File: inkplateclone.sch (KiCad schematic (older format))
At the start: 43 parts, among them J1 ED060SC7, J2 Conn_01x16_Male, U1 TPS65186, U2 ED097OC1, U3 MCP23017_SO

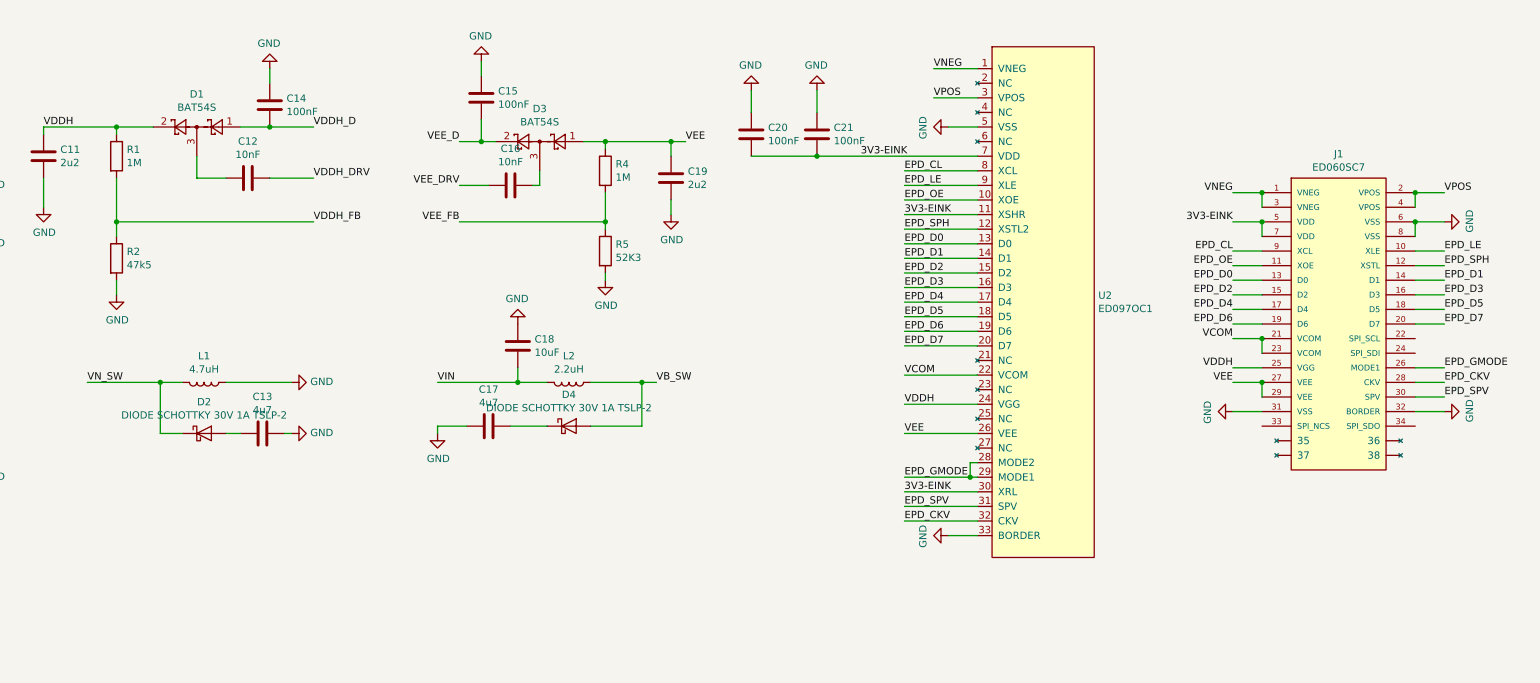
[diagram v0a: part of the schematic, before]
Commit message: added SPI pullup resistors for the 6inch display
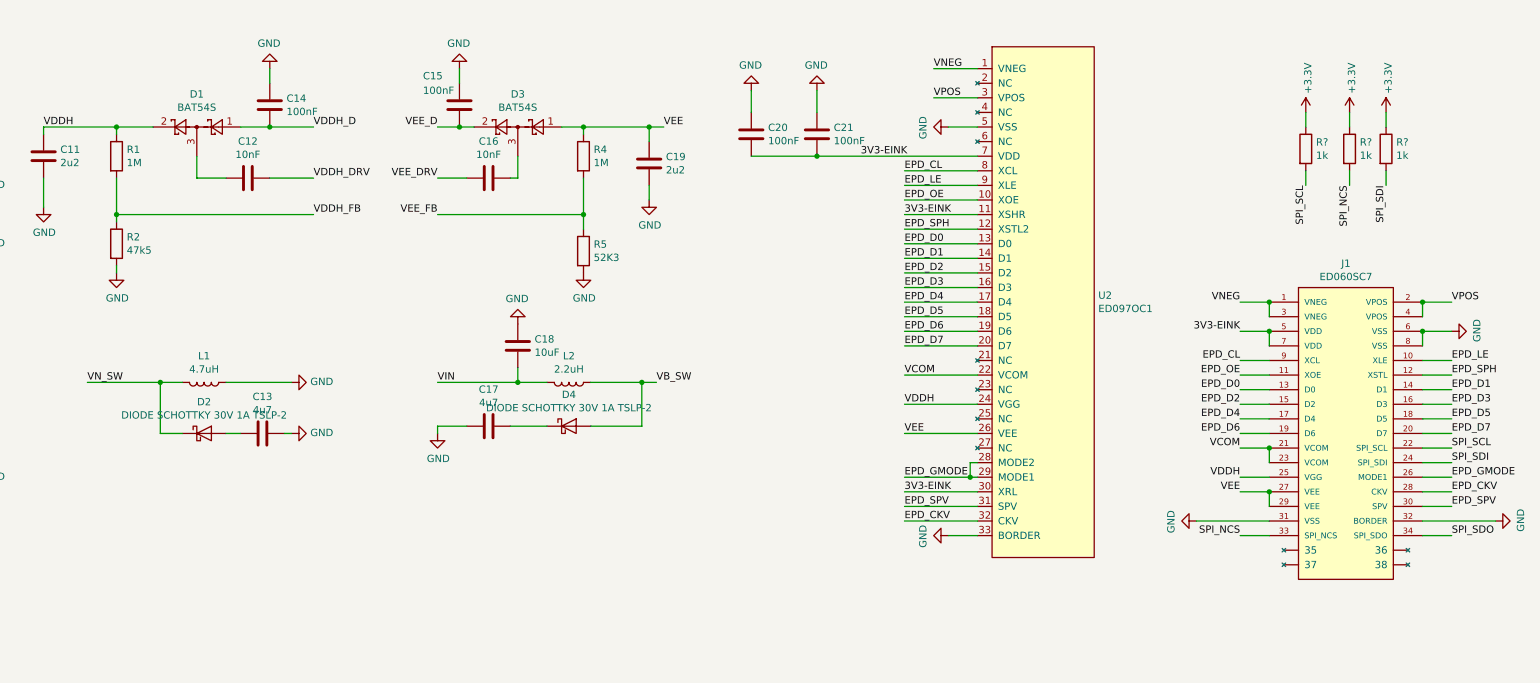
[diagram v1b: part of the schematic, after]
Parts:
- added R? (x3): 1k, Resistor_SMD:R_0805_2012Metric, symbol Device:R
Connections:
- net labels added: SPI_NCS, SPI_SCL, SPI_SDI, SPI_SDO
- wire segments 212 -> 220
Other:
- moved on the sheet: C15, C16, C19, D3, J1, R2, R4, R5

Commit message: wiring up the Wrover, WIP
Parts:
- added C23: 10uF, Capacitor_SMD:C_1206_3216Metric, symbol Device:C
- added C24: 2u2, Capacitor_SMD:C_0805_2012Metric, symbol Device:C
- added C25, C27: 68uF, 6.3v, Capacitor_Tantalum_SMD:CP_EIA-3528-15_AVX-H_Pad1.50x2.35mm_HandSolder, symbol Device:CP
- added C26, C28: 100nF, Capacitor_SMD:C_0805_2012Metric, symbol Device:C
- added U4: ESP32-WROVER, Wrover:ESP32-WROVER, symbol Wrover:ESP32-WROVER
- J1: footprint PANASONIC_AXT334124 -> inkplateclone:PANASONIC_AXT334124
- gave numbers to parts that had none: 3
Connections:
- net labels added: RST, RXD, TXD
- wire segments 220 -> 254

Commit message: ripped up and made a mess but its cool. Also added cooling pad underneath TPS56186 chip
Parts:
- removed J2: Conn_01x16_Male, Connector_PinSocket_2.54mm:PinSocket_1x16_P2.54mm_Horizontal, symbol Connector:Conn_01x16_Male
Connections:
- wire segments 254 -> 238
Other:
- moved on the sheet: C23, C24, C25, C26, C27, C28, U4

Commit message: added usb C-serial and fixed errors in the tps65186 part of the schematic
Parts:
- added C29: 100nF, Capacitor_SMD:C_0805_2012Metric, symbol Device:C
- added J2: USB_C_Receptacle_USB2.0, Connector_USB:USB_C_Receptacle_HRO_TYPE-C-31-M-12, symbol Connector:USB_C_Receptacle_USB2.0
- added Q1, Q2: Q_NMOS_GSD, Package_TO_SOT_SMD:SOT-23, symbol Device:Q_NMOS_GSD
- added R13, R14: 5.1K, Resistor_SMD:R_0805_2012Metric, symbol Device:R
- added R15, R16, R17, R18: 10K, Resistor_SMD:R_0805_2012Metric, symbol Device:R
- added U5: CH340C, Package_SO:SOIC-16_3.9x9.9mm_P1.27mm, symbol Interface_USB:CH340G
- U1: footprint Package_DFN_QFN:QFN-48-1EP_7x7mm_P0.5mm_EP5.3x5.3mm -> TP56186:QFN-48-1EP_7x7mm_P0.5mm_EP5.3x5.3mm_ThermalVias
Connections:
- net +3V3: now also R17.2, R18.2
- net EPD_CL: now also Q2.3 (D), R18.1
- net GND: now also J1.~ (38), C29.1, J2.A1 (GND), J2.A12 (GND), J2.B1 (GND), J2.B12 (GND), J2.S1 (SHIELD), R13.1, R14.1, U5.1 (GND)
- net RST: now also Q1.3 (D), R17.1
- net VB: now also C17.1, D4.1 (K)
- net VIN: now also C4.1, U1.10 (VIN)
- net VN: now also C13.2, D2.2 (A)
- net RXD renamed ESP_RXD
- net ESP_RXD: now also U5.2 (TXD)
- net TXD renamed ESP_TXD
- net ESP_TXD: now also U5.3 (RXD)
- new net: J2.A5 (CC1), R13.2
- new net: J2.B5 (CC2), R14.2
- new net: Q2.1 (G), R16.1
- new net: Q1.1 (G), R15.1
- new net +5V: C29.2, J2.A4 (VBUS), J2.A9 (VBUS), J2.B4 (VBUS), J2.B9 (VBUS), U5.16 (VCC)
- new net SER_DTR: Q2.2 (S), R15.2, U5.13 (~DTR)
- new net SER_RTS: Q1.2 (S), R16.2, U5.14 (~RTS)
- new net USB_DN: J2.A7 (D-), J2.B7 (D-), U5.6 (UD-)
- new net USB_DP: J2.A6 (D+), J2.B6 (D+), U5.5 (UD+)
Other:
- moved on the sheet: C22, R8, R9, U3

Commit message: added ideal diode and 3.3v circuit. Battery stuff and inputs still todo
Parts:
- added C30, C32, C33, C35: 4u7, Capacitor_SMD:C_0805_2012Metric, symbol Device:C
- added C31, C34: 100nF, Capacitor_SMD:C_0805_2012Metric, symbol Device:C
- added D5: BAT20JFILM, Diode_SMD:D_SOD-323, symbol Device:D_Schottky
- added Q3: Q_PMOS_GSD, Package_TO_SOT_SMD:SOT-23, symbol Device:Q_PMOS_GSD
- added R19: 10K, Resistor_SMD:R_0805_2012Metric, symbol Device:R
- added U6: AMS1117-3.3, Package_TO_SOT_SMD:SOT-223-3_TabPin2, symbol Regulator_Linear:AMS1117-3.3
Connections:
- net +3V3: now also C33.2, C34.2, C35.2, U6.2 (VO)
- net +5V: now also D5.2 (A), Q3.1 (G), R19.2
- net GND: now also C30.1, C31.1, C32.1, C33.1, C34.1, C35.1, R19.1, U6.1 (GND)
- net VIN renamed VCC
- net VCC: now also C30.2, C31.2, C32.2, D5.1 (K), Q3.2 (S), U6.3 (VI)
- new net VBAT: Q3.3 (D)
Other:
- note added: "Ideal Diode"
- note added: "todo: battery circuit, inputs, battery connector\n"
- moved on the sheet: C22, C23, C24, C25, C26, C27, C28, J1, R10, R11, R12, R8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

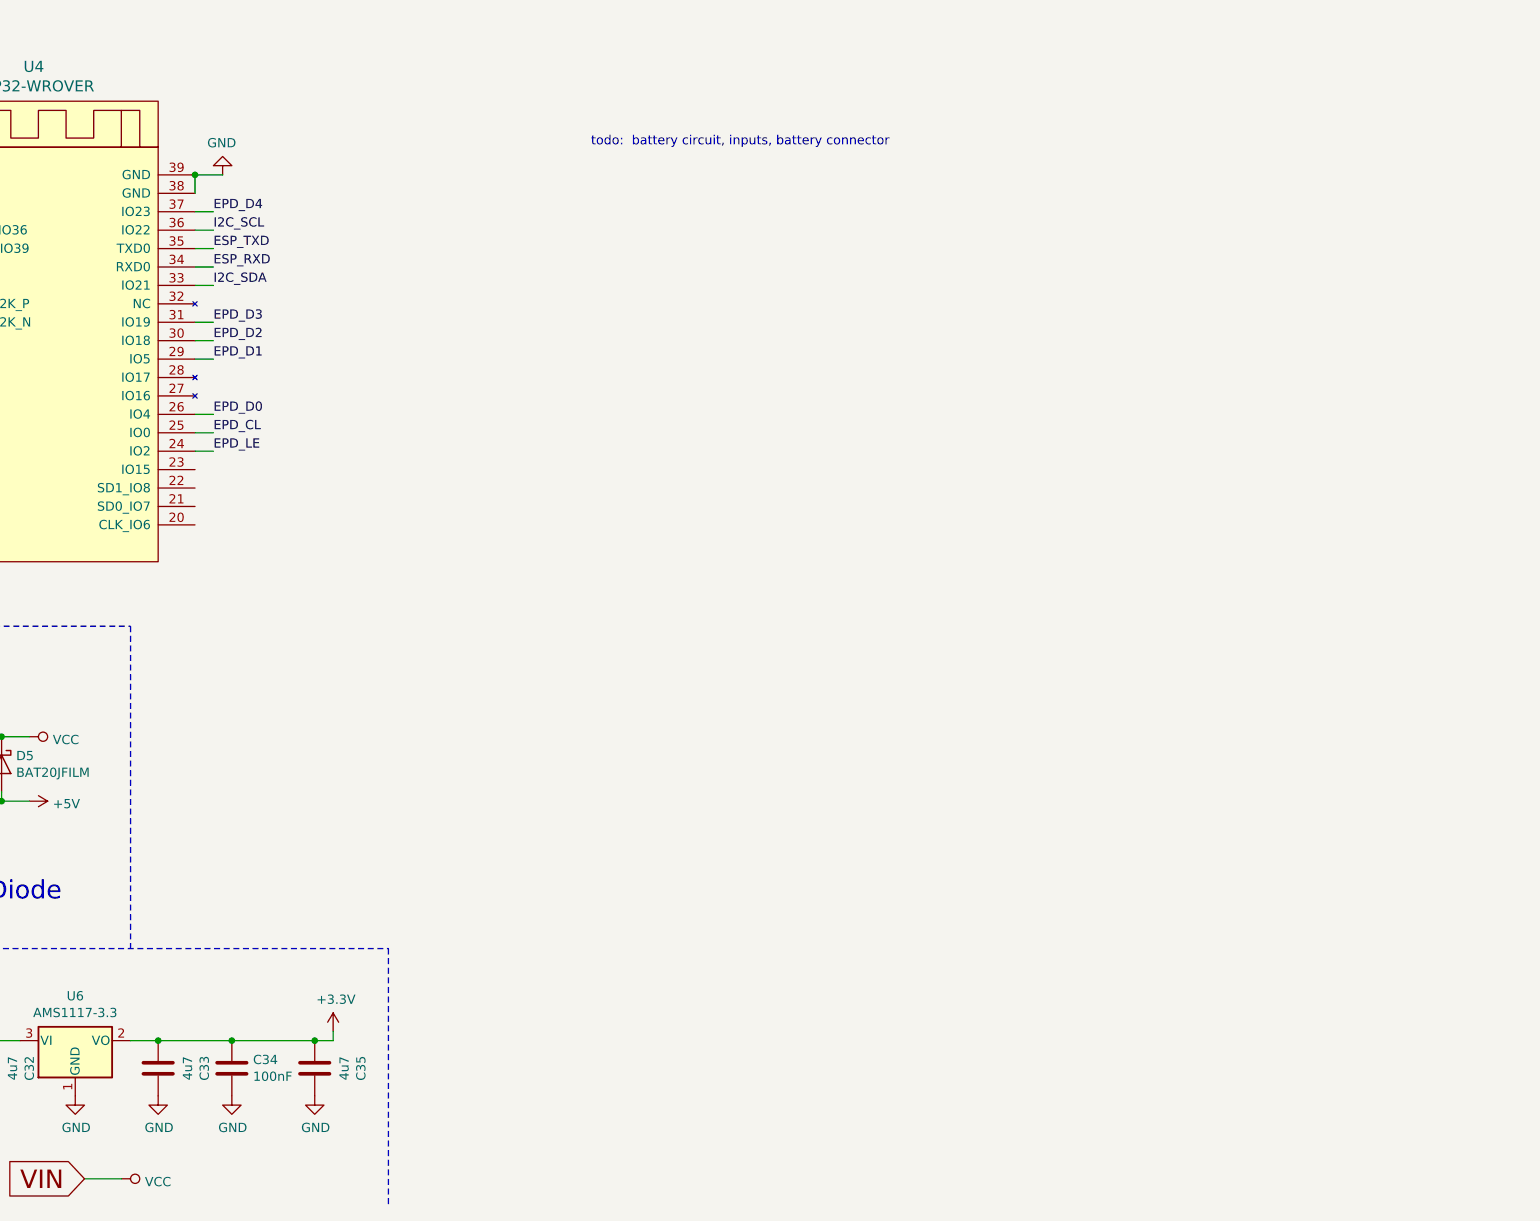
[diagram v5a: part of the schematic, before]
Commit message: added charger and protection, need to verify.
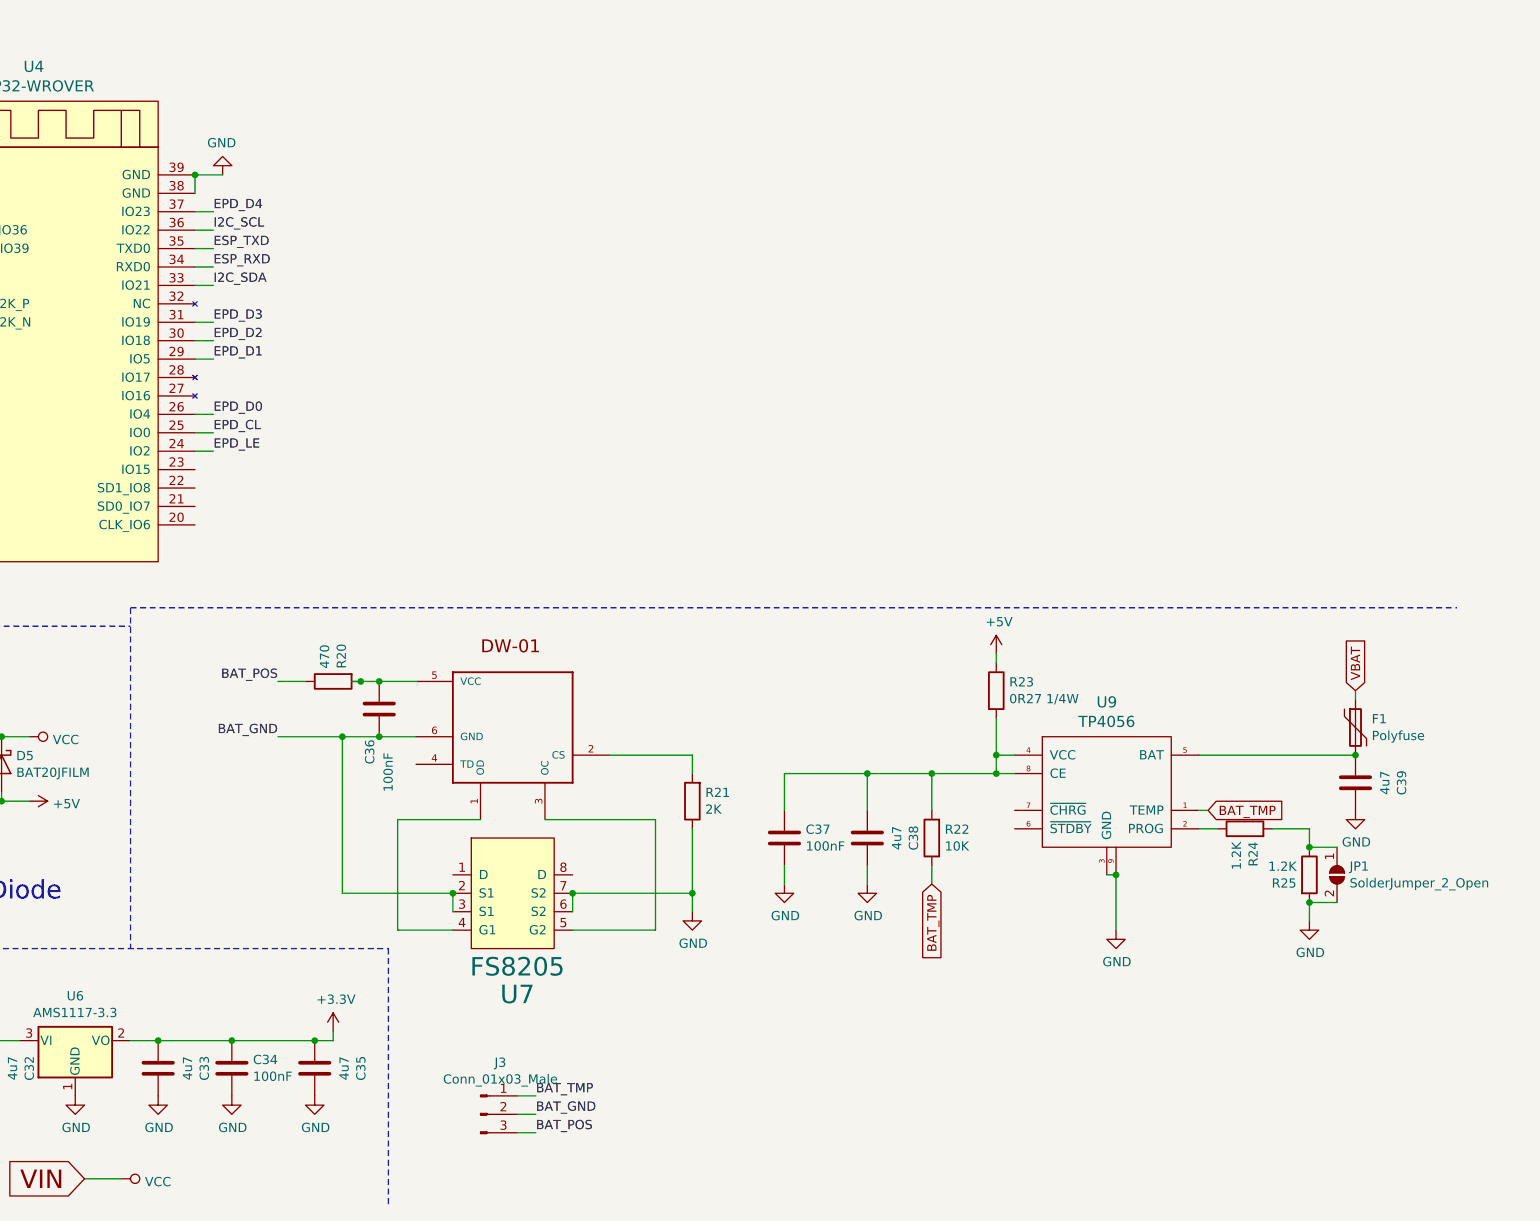
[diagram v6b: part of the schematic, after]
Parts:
- added C36, C37: 100nF, Capacitor_SMD:C_0805_2012Metric, symbol Device:C
- added C38, C39: 4u7, Capacitor_SMD:C_0805_2012Metric, symbol Device:C
- added F1: Polyfuse, Fuse:Fuse_1206_3216Metric, symbol Device:Polyfuse
- added J3: Conn_01x03_Male, Connector_JST:JST_PH_S3B-PH-SM4-TB_1x03-1MP_P2.00mm_Horizontal, symbol Connector:Conn_01x03_Male
- added JP1: SolderJumper_2_Open, Jumper:SolderJumper-2_P1.3mm_Open_Pad1.0x1.5mm, symbol Jumper:SolderJumper_2_Open
- added R20: 470, Resistor_SMD:R_0805_2012Metric, symbol Device:R
- added R21: 2K, Resistor_SMD:R_0805_2012Metric, symbol Device:R
- added R22: 10K, Resistor_SMD:R_0805_2012Metric, symbol Device:R
- added R23: 0R27 1/4W, Resistor_SMD:R_1206_3216Metric, symbol Device:R
- added R24, R25: 1.2K, Resistor_SMD:R_0805_2012Metric, symbol Device:R
- added U7: FS8205, Package_SO:TSSOP-8_4.4x3mm_P0.65mm, symbol fs8205:FS8205
- added U8: DW-01, Package_TO_SOT_SMD:SOT-23-6, symbol DW01:DW-01
- added U9: TP4056, Package_SO:SOIC-8-1EP_3.9x4.9mm_P1.27mm_EP2.29x3mm, symbol TP4056:TP4056
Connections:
- net +5V: now also R23.1
- net GND: now also C37.1, C38.1, C39.1, JP1.2 (B), R21.1, R25.2, U7.6 (S2), U7.7 (S2), U9.3 (GND), U9.9
- net VBAT: now also F1.1
- new net: R24.1, U9.2 (PROG)
- new net: C37.2, C38.2, R22.2, R23.2, U9.4 (VCC), U9.8 (CE)
- new net: C39.2, F1.2, U9.5 (BAT)
- new net: U7.4 (G1), U8.1 (OD)
- new net: R21.2, U8.2 (CS)
- new net: U7.5 (G2), U8.3 (OC)
- new net: C36.2, R20.2, U8.5 (VCC)
- new net: JP1.1 (A), R24.2, R25.1
- new net BAT_GND: C36.1, J3.2 (Pin_2), U7.2 (S1), U7.3 (S1), U8.6 (GND)
- new net BAT_POS: J3.3 (Pin_3), R20.1
- new net BAT_TMP: J3.1 (Pin_1), R22.1, U9.1 (TEMP)
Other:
- note removed: "todo: battery circuit, inputs, battery connector\n"

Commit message: done some ratsnests
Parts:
- added F2: Polyfuse, Fuse:Fuse_1206_3216Metric, symbol Device:Polyfuse
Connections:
- net +5V: now also F2.1; no longer J2.A4 (VBUS), J2.A9 (VBUS), J2.B4 (VBUS), J2.B9 (VBUS)
- net GND: no longer J1.~ (38)
- new net: F2.2, J2.A4 (VBUS), J2.A9 (VBUS), J2.B4 (VBUS), J2.B9 (VBUS)
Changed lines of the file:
@@
 	1    0    0    -1
-$EndComp
-$Comp
-L power:GND #PWR0107
-U 1 1 5EB96A29
-P 15100 4000
-F 0 "#PWR0107" H 15100 3750 50  0001 C CNN
-F 1 "GND" H 15105 3827 50  0000 C CNN
-F 2 "" H 15100 4000 50  0001 C CNN
-F 3 "" H 15100 4000 50  0001 C CNN
-	1    15100 4000
-	0    -1   -1   0
-$EndComp
-$Comp
-L power:GND #PWR0108
-U 1 1 5EB96DC7
-P 15100 4100
-F 0 "#PWR0108" H 15100 3850 50  0001 C CNN
-F 1 "GND" H 15105 3927 50  0000 C CNN
-F 2 "" H 15100 4100 50  0001 C CNN
-F 3 "" H 15100 4100 50  0001 C CNN
-	1    15100 4100
-	0    -1   -1   0
-$EndComp
-$Comp
-L power:GND #PWR0111
-U 1 1 5EB96FC2
-P 14200 4000
-F 0 "#PWR0111" H 14200 3750 50  0001 C CNN
-F 1 "GND" H 14205 3827 50  0000 C CNN
-F 2 "" H 14200 4000 50  0001 C CNN
-F 3 "" H 14200 4000 50  0001 C CNN
-	1    14200 4000
-	0    1    1    0
 $EndComp
 Wire Wire Line
 	14250 4000 14200 4000
-$Comp
-L power:GND #PWR0112
-U 1 1 5EC3177A
-P 14200 4100
-F 0 "#PWR0112" H 14200 3850 50  0001 C CNN
-F 1 "GND" H 14205 3927 50  0000 C CNN
-F 2 "" H 14200 4100 50  0001 C CNN
-F 3 "" H 14200 4100 50  0001 C CNN
-	1    14200 4100
-	0    1    1    0
-$EndComp
 Wire Wire Line
 	14200 4100 14250 4100
@@
 L power:+5V #PWR048
 U 1 1 5ED27104
-P 2200 8900
-F 0 "#PWR048" H 2200 8750 50  0001 C CNN
-F 1 "+5V" H 2215 9073 50  0000 C CNN
-F 2 "" H 2200 8900 50  0001 C CNN
-F 3 "" H 2200 8900 50  0001 C CNN
-	1    2200 8900
+P 2200 8600
+F 0 "#PWR048" H 2200 8450 50  0001 C CNN
+F 1 "+5V" H 2215 8773 50  0000 C CNN
+F 2 "" H 2200 8600 50  0001 C CNN
+F 3 "" H 2200 8600 50  0001 C CNN
+	1    2200 8600
 	1    0    0    -1
 $EndComp
@@
 Ideal Diode
 Wire Notes Line
-	6750 11200 6750 8050
+	6750 11150 6750 8000
 Wire Notes Line
 	500  4350 16050 4350
 Wire Notes Line
-	3600 4350 3600 8050
+	3600 4350 3600 7950
 $Comp
 L Regulator_Linear:AMS1117-3.3 U6
@@
 Wire Wire Line
 	8800 11050 8600 11050
-Wire Notes Line
-	500  8050 8850 8050
 Wire Notes Line
 	10250 9800 10250 11200
@@
 	12850 9350 12850 9450
 Wire Notes Line
-	8850 7950 16050 7950
+	8850 7950 8850 9800
 Wire Notes Line
-	8850 7950 8850 9800
+	500  7950 16050 7950
+$Comp
+L Device:Polyfuse F2
+U 1 1 5F977BD5
+P 2200 8750
+F 0 "F2" H 2288 8796 50  0000 L CNN
+F 1 "Polyfuse" H 2288 8705 50  0000 L CNN
+F 2 "Fuse:Fuse_1206_3216Metric" H 2250 8550 50  0001 L CNN
+F 3 "~" H 2200 8750 50  0001 C CNN
+	1    2200 8750
+	1    0    0    -1
+$EndComp
 $EndSCHEMATC

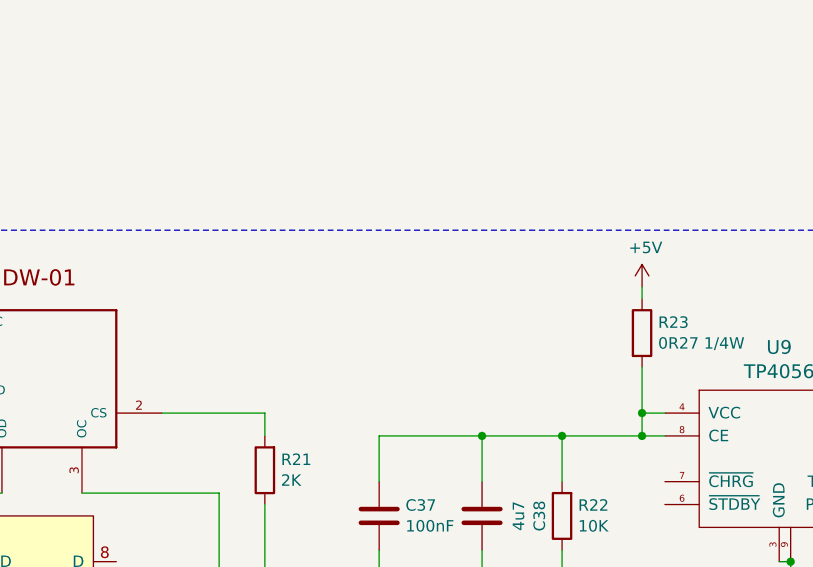
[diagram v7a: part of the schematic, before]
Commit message: more ratsnest, push before sleep
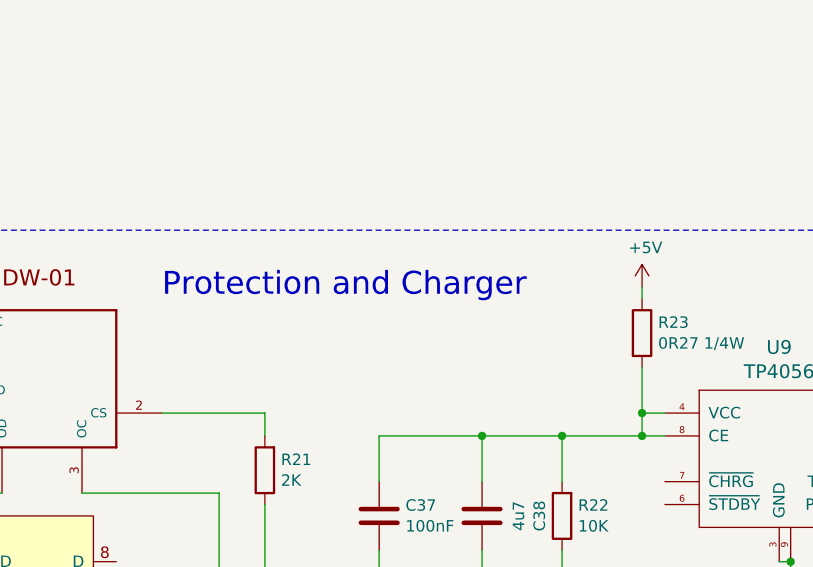
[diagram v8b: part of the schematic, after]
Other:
- note added: "Protection and Charger"
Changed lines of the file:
@@
 	1    0    0    -1
 $EndComp
+Text Notes 11450 8250 0    100  ~ 0
+Protection and Charger
 $EndSCHEMATC
